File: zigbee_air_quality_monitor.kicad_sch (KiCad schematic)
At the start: 30 parts, among them J1 USB_C_Receptacle_USB2.0, J2 QWIIC, J3 Conn_02x02_Odd_Even, SW1 PAIR_BTN, SW2 USER_BTN, U1 USBLC6-2SC6, U2 BT840, U3 XC6206P332MR, U4 SCD41-D-R2, U6 TXS0102DCU

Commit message: Routing done, via stitching done
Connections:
- no-connect marks 47 -> 46
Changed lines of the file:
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@@
   (no_connect (at 108.966 186.944))
   (no_connect (at 51.816 78.486))
-  (no_connect (at 347.472 60.452))
   (no_connect (at 149.606 184.404))
   (no_connect (at 149.606 156.464))

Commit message: Fixed QWIIC connector footprint and model
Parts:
- J2: footprint Connector_JST:JST_SH_BM04B-SRSS-TB_1x04-1MP_P1.00mm_Vertical -> Connector_JST:JST_SH_SM04B-SRSS-TB_1x04-1MP_P1.00mm_Horizontal
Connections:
- net +3.3V: now also J2.2 (Pin_2); no longer J2.3 (Pin_3)
- net GND: now also J2.1 (Pin_1); no longer J2.4 (Pin_4)
- net I2C_SCL_3V3: now also J2.4 (Pin_4); no longer J2.1 (Pin_1)
- net I2C_SDA_3V3: now also J2.3 (Pin_3); no longer J2.2 (Pin_2)
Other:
- note added: "Internal 10k pullups + ESD protection."
- note removed: "Internal 10k pullups."
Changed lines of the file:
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@@
+    (stroke (width 0) (type default))
+  )
+  (wire (pts (xy 378.46 126.492) (xy 378.46 135.89))
     (stroke (width 0) (type default))
   )
@@
     (stroke (width 0) (type default))
   )
-  (wire (pts (xy 380.238 131.572) (xy 378.46 131.572))
+  (wire (pts (xy 376.682 129.032) (xy 380.238 129.032))
     (stroke (width 0) (type default))
   )
@@
     (stroke (width 0) (type default))
   )
+  (wire (pts (xy 380.238 126.492) (xy 378.46 126.492))
+    (stroke (width 0) (type default))
+  )
   (wire (pts (xy 99.568 62.484) (xy 113.03 62.484))
     (stroke (width 0) (type default))
@@
     (stroke (width 0) (type default))
   )
-  (wire (pts (xy 378.46 124.46) (xy 378.46 131.572))
-    (stroke (width 0) (type default))
-  )
   (wire (pts (xy 87.376 176.784) (xy 87.376 181.102))
     (stroke (width 0) (type default))
@@
     (stroke (width 0) (type default))
   )
-  (wire (pts (xy 375.158 126.492) (xy 380.238 126.492))
+  (wire (pts (xy 375.158 134.112) (xy 380.238 134.112))
     (stroke (width 0) (type default))
   )
@@
     (stroke (width 0) (type default))
   )
-  (wire (pts (xy 378.46 134.112) (xy 380.238 134.112))
-    (stroke (width 0) (type default))
-  )
   (polyline (pts (xy 273.05 54.864) (xy 242.316 54.864))
     (stroke (width 0) (type default))
@@
     (stroke (width 0) (type default))
   )
-  (wire (pts (xy 378.46 135.89) (xy 378.46 134.112))
-    (stroke (width 0) (type default))
-  )
   (polyline (pts (xy 225.298 118.618) (xy 225.298 153.924))
     (stroke (width 0) (type default))
@@
     (stroke (width 0) (type default))
   )
-  (wire (pts (xy 375.158 129.032) (xy 380.238 129.032))
+  (wire (pts (xy 375.158 131.572) (xy 380.238 131.572))
     (stroke (width 0) (type default))
   )
@@
     (stroke (width 0) (type default))
   )
+  (wire (pts (xy 376.682 124.206) (xy 376.682 129.032))
+    (stroke (width 0) (type default))
+  )
   (wire (pts (xy 270.51 131.064) (xy 272.288 131.064))
     (stroke (width 0) (type default))
@@
     (fill (type none))
   )
-  (text "Internal 10k pullups." (at 300.99 163.322 0)
+  (text "Internal 10k pullups + ESD protection." (at 300.99 163.322 0)
     (effects (font (size 1.27 1.27)) (justify left bottom))
   )
@@
     (effects (font (size 2 2) (thickness 0.4) bold) (justify left bottom))
   )
-  (label "I2C_SDA_3V3" (at 375.158 129.032 180) (fields_autoplaced)
+  (label "I2C_SDA_3V3" (at 375.158 131.572 180) (fields_autoplaced)
     (effects (font (size 1.27 1.27)) (justify right bottom))
   )
@@
     (effects (font (size 1.27 1.27)) (justify left bottom))
   )
-  (label "I2C_SCL_3V3" (at 375.158 126.492 180) (fields_autoplaced)
+  (label "I2C_SCL_3V3" (at 375.158 134.112 180) (fields_autoplaced)
     (effects (font (size 1.27 1.27)) (justify right bottom))
   )
@@
       (effects (font (size 1.27 1.27)) (justify right))
     )
-    (property "Footprint" "Connector_JST:JST_SH_BM04B-SRSS-TB_1x04-1MP_P1.00mm_Vertical" (at 385.318 129.032 0)
+    (property "Footprint" "Connector_JST:JST_SH_SM04B-SRSS-TB_1x04-1MP_P1.00mm_Horizontal" (at 385.318 129.032 0)
       (effects (font (size 1.27 1.27)) hide)
     )
@@
     )
   )
-  (symbol (lib_id "power:+3.3V") (at 378.46 124.46 0) (unit 1)
-    (in_bom yes) (on_board yes) (dnp no)
-    (property "Reference" "#PWR025" (at 378.46 128.27 0)
-      (effects (font (size 1.27 1.27)) hide)
-    )
-    (property "Value" "+3.3V" (at 378.46 120.65 0)
-      (effects (font (size 1.27 1.27)))
-    )
-    (property "Footprint" "" (at 378.46 124.46 0)
-      (effects (font (size 1.27 1.27)) hide)
-    )
-    (property "Datasheet" "" (at 378.46 124.46 0)
-      (effects (font (size 1.27 1.27)) hide)
-    )
+  (symbol (lib_id "power:+3.3V") (at 376.682 124.206 0) (unit 1)
+    (in_bom yes) (on_board yes) (dnp no)
+    (property "Reference" "#PWR025" (at 376.682 128.016 0)
+      (effects (font (size 1.27 1.27)) hide)
+    )
+    (property "Value" "+3.3V" (at 376.682 120.396 0)
+      (effects (font (size 1.27 1.27)))
+    )
+    (property "Footprint" "" (at 376.682 124.206 0)
+      (effects (font (size 1.27 1.27)) hide)
+    )
+    (property "Datasheet" "" (at 376.682 124.206 0)
+      (effects (font (size 1.27 1.27)) hide)
+    )

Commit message: Changed supply voltage for WS2812-2020 LED to 5V
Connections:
- net +3.3V: no longer D3.1 (VDD)
- net VCC: now also D3.1 (VDD)
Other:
- moved on the sheet: C10, C11, J2, U4, U6

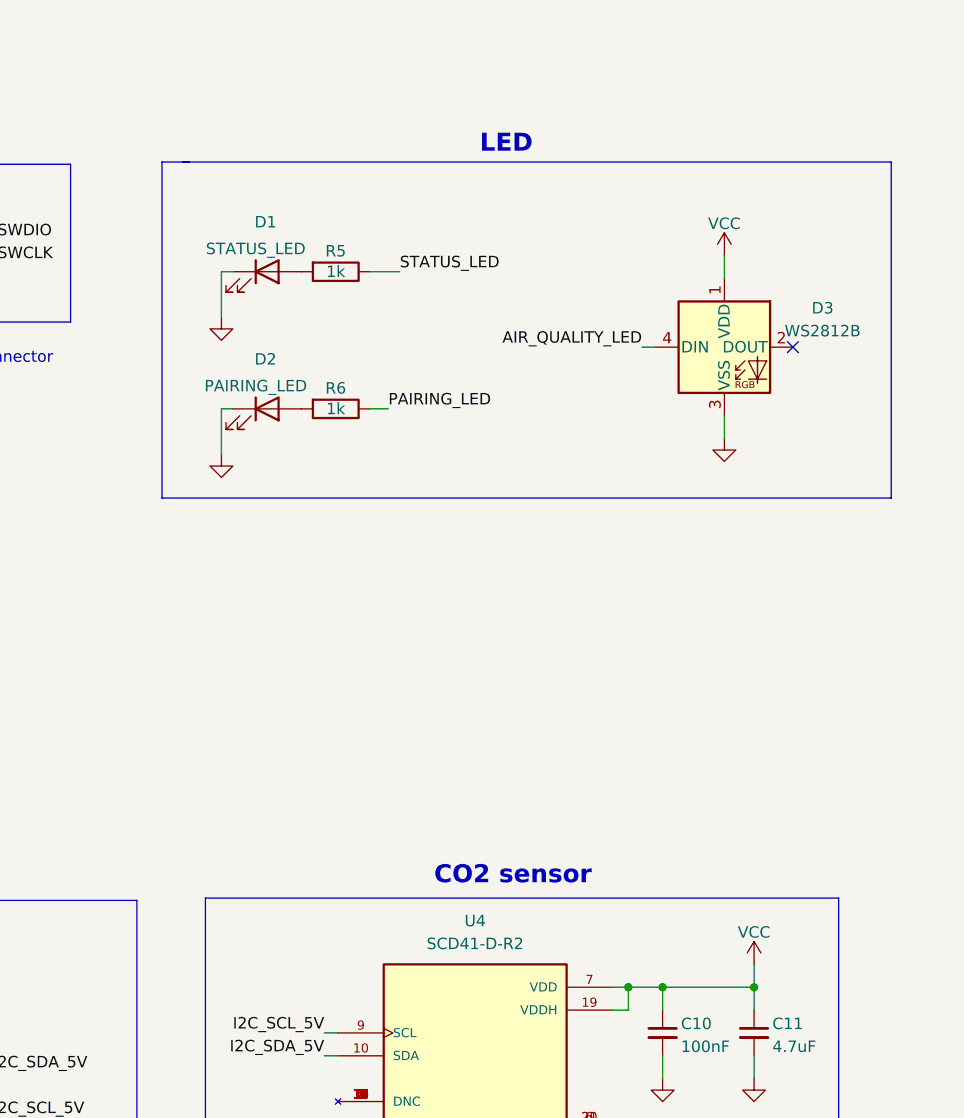
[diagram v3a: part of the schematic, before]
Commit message: LED exact name, SCD40 exact name
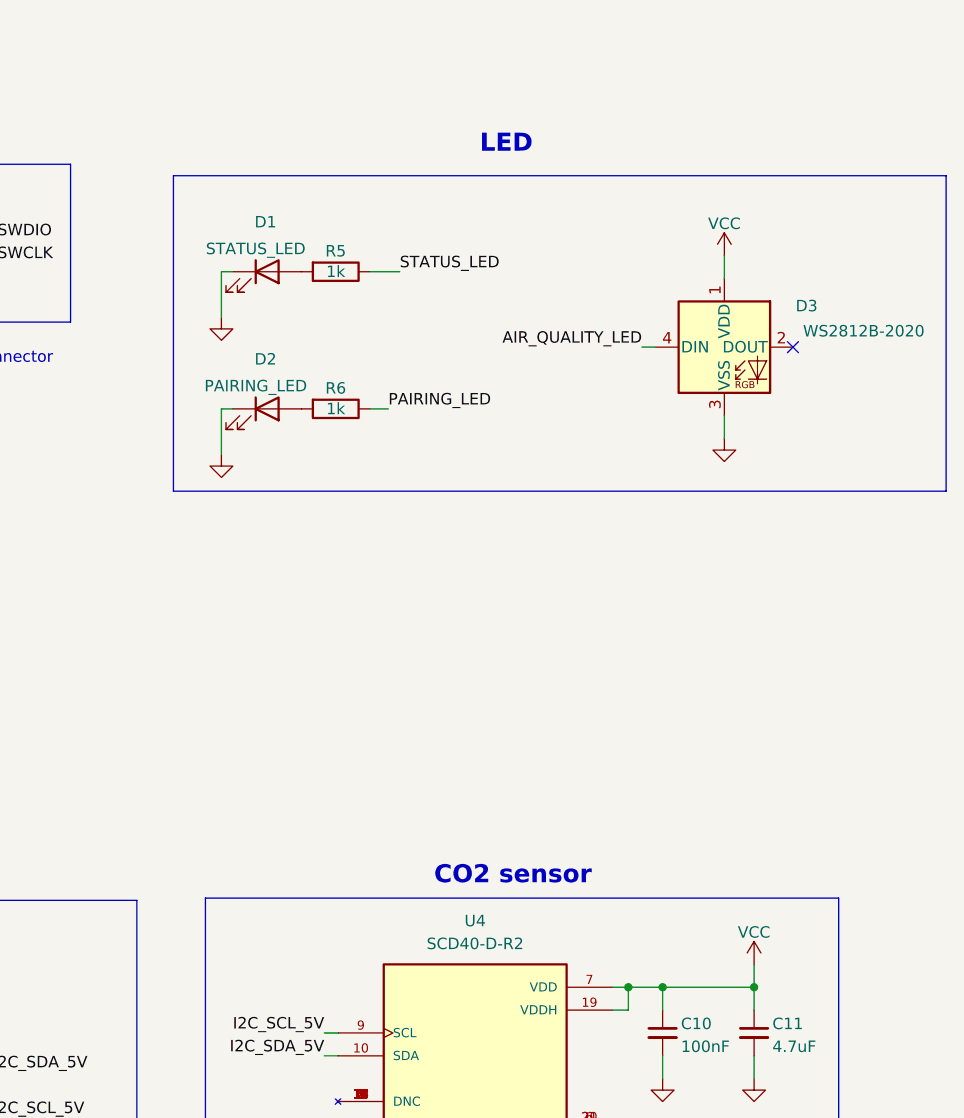
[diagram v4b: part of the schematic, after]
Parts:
- D3: value WS2812B -> WS2812B-2020
- U4: value SCD41-D-R2 -> SCD40-D-R2
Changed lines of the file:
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@@
-    (stroke (width 0) (type default))
-  )
-  (polyline (pts (xy 283.21 37.084) (xy 283.21 74.422))
     (stroke (width 0) (type default))
   )
@@
     (stroke (width 0) (type default))
   )
-  (polyline (pts (xy 364.236 74.422) (xy 283.21 74.422))
-    (stroke (width 0) (type default))
-  )
   (wire (pts (xy 36.576 86.106) (xy 36.576 87.122))
     (stroke (width 0) (type default))
@@
     (stroke (width 0) (type default))
   )
-  (polyline (pts (xy 285.496 37.084) (xy 364.236 37.084))
-    (stroke (width 0) (type default))
-  )
   (wire (pts (xy 149.606 133.604) (xy 151.892 133.604))
     (stroke (width 0) (type default))
@@
     (stroke (width 0) (type default))
   )
-  (polyline (pts (xy 283.21 37.084) (xy 286.258 37.084))
-    (stroke (width 0) (type default))
-  )
   (wire (pts (xy 335.026 131.318) (xy 335.026 128.778))
     (stroke (width 0) (type default))
@@
     (stroke (width 0) (type default))
   )
-  (polyline (pts (xy 364.236 37.084) (xy 364.236 74.422))
-    (stroke (width 0) (type default))
-  )
   (polyline (pts (xy 288.036 118.872) (xy 288.036 154.178))
     (stroke (width 0) (type default))
@@
   (wire (pts (xy 345.694 65.278) (xy 345.694 67.818))
     (stroke (width 0) (type default))
+  )
+  (rectangle (start 284.48 38.608) (end 370.332 73.66)
+    (stroke (width 0) (type default))
+    (fill (type none))
   )
   (rectangle (start 225.044 119.126) (end 280.416 161.29)
@@
   )
   (symbol (lib_id "LED:WS2812B") (at 345.694 57.658 0) (unit 1)
-    (in_bom yes) (on_board yes) (dnp no) (fields_autoplaced)
-    (property "Reference" "D3" (at 356.616 53.3273 0)
-      (effects (font (size 1.27 1.27)))
-    )
-    (property "Value" "WS2812B" (at 356.616 55.8673 0)
+    (in_bom yes) (on_board yes) (dnp no)
+    (property "Reference" "D3" (at 354.838 53.086 0)
+      (effects (font (size 1.27 1.27)))
+    )
+    (property "Value" "WS2812B-2020" (at 361.188 55.88 0)
       (effects (font (size 1.27 1.27)))
     )
@@
       (effects (font (size 1.27 1.27)))
     )
-    (property "Value" "SCD41-D-R2" (at 318.008 123.952 0)
-      (effects (font (size 1.27 1.27)))
-    )
+    (property "Value" "SCD40-D-R2" (at 318.008 123.952 0)
+      (effects (font (size 1.27 1.27)))
+    )

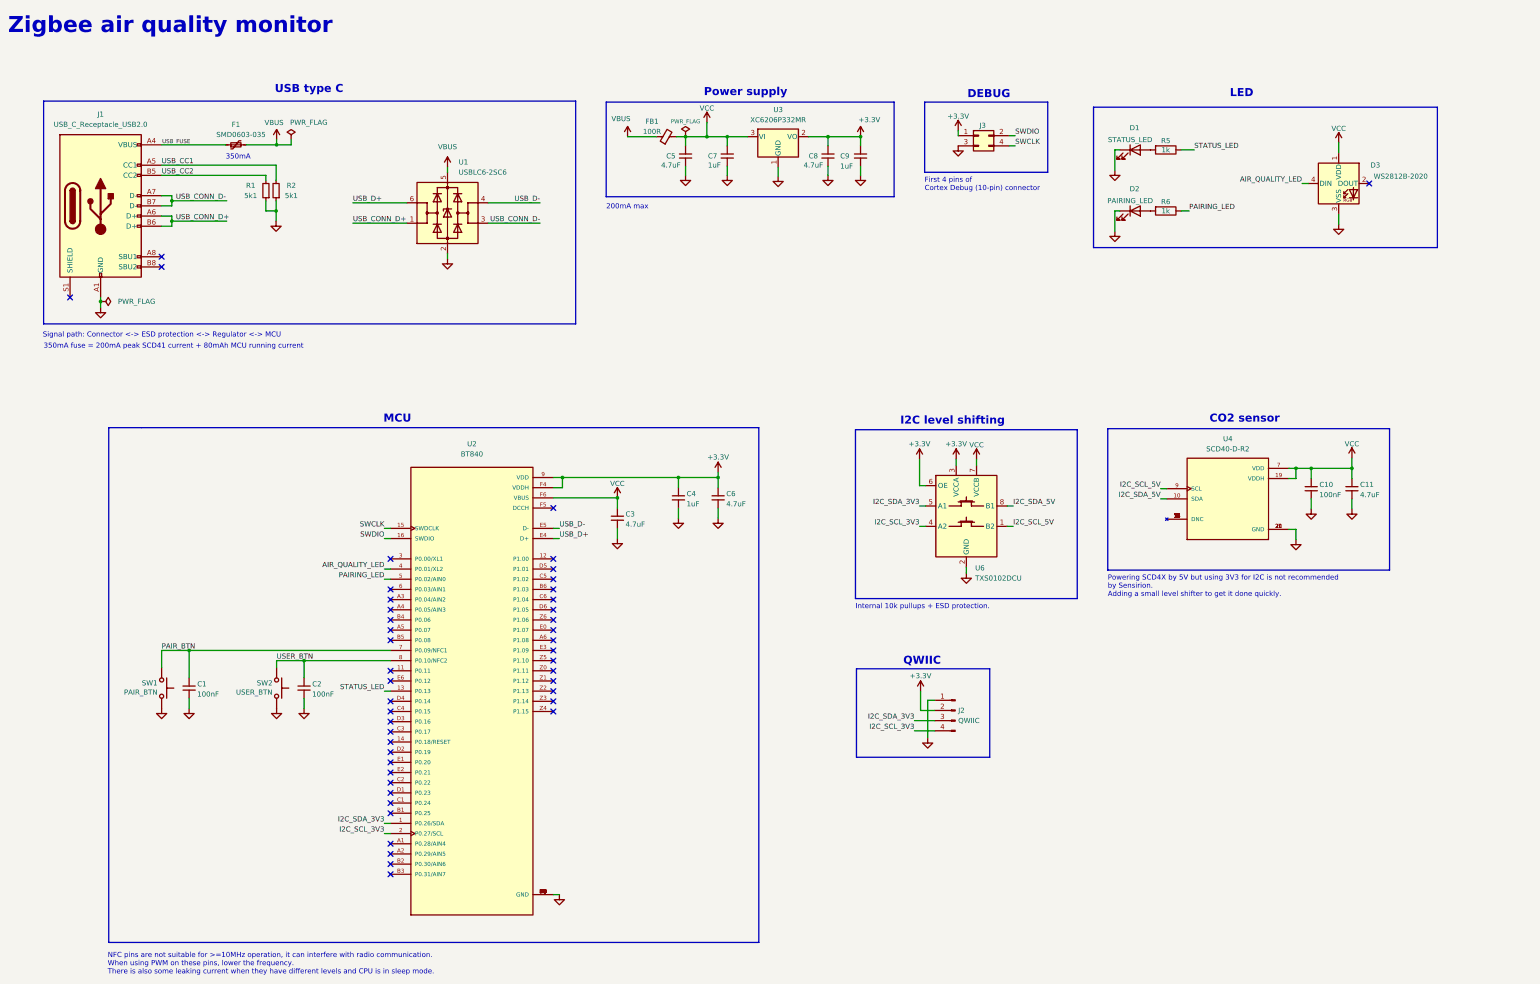
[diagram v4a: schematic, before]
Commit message: rev2
Fixed RGB LED footprint, removed problematic button caps, cleaning
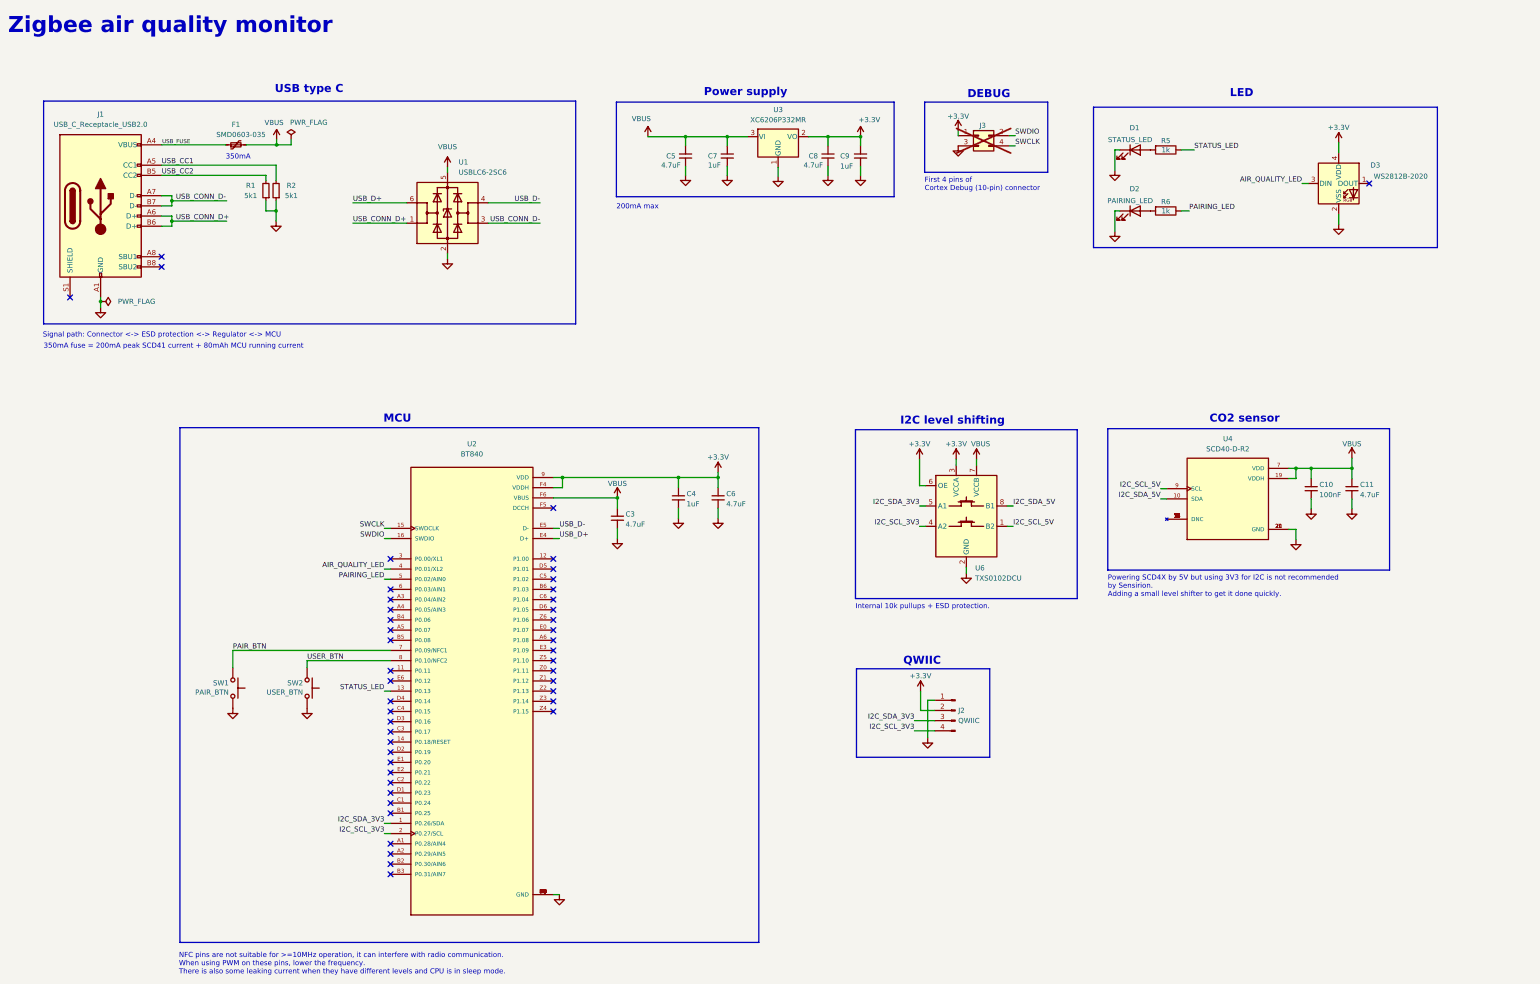
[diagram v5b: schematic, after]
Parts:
- removed C1, C2: 100nF, Capacitor_SMD:C_0603_1608Metric, symbol Device:C_Small
- removed FB1: 100R, Inductor_SMD:L_0603_1608Metric, symbol Device:FerriteBead_Small
- C10: LCSC Part (none) -> C14663
- C11, C3, C6: LCSC Part (none) -> C19666
- C4: LCSC Part (none) -> C15849
- C5, C8: LCSC Part C1705 -> C19666
- C7, C9: LCSC Part C1592 -> C15849
- D3: footprint LED_SMD:LED_WS2812B-2020_PLCC4_2.0x2.0mm -> LED_SMD:LED_WS2812B_PLCC4_5.0x5.0mm_P3.2mm
- F1: LCSC Part (none) -> C910818
- J3: now not fitted
- R1, R2: LCSC Part C105580 -> C23186
- R5, R6: LCSC Part (none) -> C21190
- U2: DPM (none) -> 1914-1018-1-ND
- U4: LCSC Part (none) -> C3659421
- U6: LCSC Part (none) -> C53434
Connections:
- net +3.3V: now also D3.4 (VDD)
- net AIR_QUALITY_LED: now also D3.3 (DIN); no longer D3.4 (DIN)
- net GND: now also D3.2 (VSS); no longer D3.3 (VSS)
- net VBUS: now also C10.1, C11.1, C3.1, C5.1, C7.1, U2.F6 (VBUS), U3.3 (VI), U4.19 (VDDH), U4.7 (VDD), U6.7 (VCCB)
- removed net VCC: C10.1, C11.1, C3.1, C5.1, C7.1, D3.1 (VDD), U2.F6 (VBUS), U3.3 (VI), U4.19 (VDDH), U4.7 (VDD), U6.7 (VCCB)
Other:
- moved on the sheet: SW1, SW2

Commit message: Manufacturing fixes
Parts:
- D1: LCSC Part (none) -> C965804
- D2: LCSC Part (none) -> C965807
- J2: LCSC Part C160404 -> C9900058894
- U2: LCSC Part (none) -> C5182373
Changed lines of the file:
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@@
+			)
+		)
+		(property "LCSC Part" "C5182373"
+			(at 129.286 184.404 0)
+			(effects
+				(font
+					(size 1.27 1.27)
+				)
+				(hide yes)
 			)
 		)
@@
 		)
 		(property "Description" ""
+			(at 294.894 64.516 0)
+			(effects
+				(font
+					(size 1.27 1.27)
+				)
+				(hide yes)
+			)
+		)
+		(property "LCSC Part" "C965807"
 			(at 294.894 64.516 0)
 			(effects
@@
 			)
 		)
-		(property "LCSC Part" "C160404"
+		(property "LCSC Part" "C9900058894"
 			(at 249.936 189.23 0)
 			(effects
@@
 			(at 294.894 49.276 0)
 			(effects
+				(font
+					(size 1.27 1.27)
+				)
+				(hide yes)
+			)
+		)
+		(property "LCSC Part" "C965804"
+			(at 294.894 49.276 0)
+			(effects
